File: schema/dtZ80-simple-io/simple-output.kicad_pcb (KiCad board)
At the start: 2 copper layers, 12 parts, among them J1 Conn_01x40, U1 74LS138, U2 74LS573, U3 74LS573, U4 74HC00, U5 HDSP-A151, U6 HDSP-A151

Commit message: Reworked Boards
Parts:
- removed U6: HDSP-A151, Display_7Segment:HDSP-A151
- added C2: 100n, Capacitor_THT:C_Disc_D4.3mm_W1.9mm_P5.00mm, F.Cu at (118.1, 188.0)
- added C3: 22pF, Capacitor_THT:C_Disc_D4.3mm_W1.9mm_P5.00mm, F.Cu at (77.5, 135.9)
- added C4: 100n, Capacitor_THT:C_Disc_D4.3mm_W1.9mm_P5.00mm, F.Cu at (111.8, 130.8)
- added C5: 100n, Capacitor_THT:C_Disc_D4.3mm_W1.9mm_P5.00mm, F.Cu at (54.6, 129.5)
- added C6: 22pF, Capacitor_THT:C_Disc_D4.3mm_W1.9mm_P5.00mm, F.Cu at (85.1, 135.9)
- added IC1: Z80SIO, Package_DIP:DIP-40_W15.24mm_Socket, F.Cu at (52.1, 135.9)
- added IC2: Z80CTC, Package_DIP:DIP-28_W15.24mm_Socket, F.Cu at (91.4, 175.3)
- added J2: 8 Bit Port, Connector_PinHeader_2.54mm:PinHeader_2x07_P2.54mm_Vertical, F.Cu at (55.9, 90.2)
- added J3: FT_232, Connector_PinHeader_2.54mm:PinHeader_1x06_P2.54mm_Vertical, F.Cu at (55.9, 101.6)
- added J4: Mini-DIN-6, package_connectors:Mini_DIN_6_TE_Connectivity, F.Cu at (161.3, 121.9)
- added Jumper1: Conn_01x02, Connector_PinHeader_2.54mm:PinHeader_1x02_P2.54mm_Vertical, F.Cu at (94.0, 106.7)
- added Q1: Q_NPN_BCE, Package_TO_SOT_THT:TO-92_HandSolder, F.Cu at (151.1, 138.4)
- added Q2: Q_NPN_BCE, Package_TO_SOT_THT:TO-92_HandSolder, F.Cu at (151.1, 146.1)
- added R10: 1k, Resistor_THT:R_Axial_DIN0204_L3.6mm_D1.6mm_P5.08mm_Horizontal, F.Cu at (123.2, 181.6)
- added R11: 5K, Resistor_THT:R_Axial_DIN0204_L3.6mm_D1.6mm_P5.08mm_Horizontal, F.Cu at (149.9, 120.7)
- added R12: 5K, Resistor_THT:R_Axial_DIN0204_L3.6mm_D1.6mm_P5.08mm_Horizontal, F.Cu at (149.9, 125.7)
- added R13: 5K, Resistor_THT:R_Axial_DIN0204_L3.6mm_D1.6mm_P5.08mm_Horizontal, F.Cu at (141.0, 142.2)
- added R14: 5K, Resistor_THT:R_Axial_DIN0204_L3.6mm_D1.6mm_P5.08mm_Horizontal, F.Cu at (141.0, 147.3)
- added R5: 10K, Resistor_THT:R_Axial_DIN0204_L3.6mm_D1.6mm_P5.08mm_Horizontal, F.Cu at (78.7, 184.2)
- added R6: 2K, Resistor_THT:R_Axial_DIN0204_L3.6mm_D1.6mm_P5.08mm_Horizontal, F.Cu at (66.0, 113.0)
- added R7: 10K, Resistor_THT:R_Axial_DIN0204_L3.6mm_D1.6mm_P5.08mm_Horizontal, F.Cu at (72.4, 144.8)
- added R8: 2K, Resistor_THT:R_Axial_DIN0204_L3.6mm_D1.6mm_P5.08mm_Horizontal, F.Cu at (61.0, 119.4)
- added R9: 2K, Resistor_THT:R_Axial_DIN0204_L3.6mm_D1.6mm_P5.08mm_Horizontal, F.Cu at (57.1, 108.0)
- added U8: 74HC245, Package_DIP:DIP-20_W7.62mm_Socket, F.Cu at (116.8, 137.2)
- added Y1: Crystal, Crystal:Crystal_HC49-U_Vertical, F.Cu at (99.1, 144.8)
- C1: value 10u -> 100n; footprint Capacitor_THT:CP_Radial_Tantal_D4.5mm_P5.00mm -> Capacitor_THT:C_Disc_D4.3mm_W1.9mm_P5.00mm
- J1: value Conn_01x40 -> RC2014Bus; footprint Connector_PinSocket_2.54mm:PinSocket_1x40_P2.54mm_Horizontal -> Connector_PinHeader_2.54mm:PinHeader_1x40_P2.54mm_Vertical
- R1: footprint Resistor_THT:R_Axial_DIN0204_L3.6mm_D1.6mm_P1.90mm_Vertical -> Resistor_THT:R_Axial_DIN0204_L3.6mm_D1.6mm_P5.08mm_Horizontal
- R2: value 1k -> 220; footprint Resistor_THT:R_Axial_DIN0204_L3.6mm_D1.6mm_P1.90mm_Vertical -> Resistor_THT:R_Axial_DIN0204_L3.6mm_D1.6mm_P5.08mm_Horizontal
- R3: value 220 -> 1M; footprint Resistor_THT:R_Axial_DIN0204_L3.6mm_D1.6mm_P1.90mm_Vertical -> Resistor_THT:R_Axial_DIN0204_L3.6mm_D1.6mm_P5.08mm_Horizontal
- R4: value 220 -> 1K; footprint Resistor_THT:R_Axial_DIN0204_L3.6mm_D1.6mm_P1.90mm_Vertical -> Resistor_THT:R_Axial_DIN0204_L3.6mm_D1.6mm_P5.08mm_Horizontal
- U1: value 74LS138 -> 74LS04; footprint Package_DIP:DIP-16_W7.62mm_Socket -> Package_DIP:DIP-14_W7.62mm_Socket
- U2: value 74LS573 -> 74LS138; footprint Package_DIP:DIP-20_W7.62mm_Socket -> Package_DIP:DIP-16_W7.62mm_Socket
- U4: value 74HC00 -> 74HC245; footprint Package_DIP:DIP-14_W10.16mm -> Package_DIP:DIP-20_W7.62mm_Socket
- U5: value HDSP-A151 -> 5161AS; footprint Display_7Segment:HDSP-A151 -> 7seg:7SegmentLED_LTS6760_LTS6780
- moved J1 147.3 mm to (162.6, 193.0), turned to 270 degrees
- moved U1 87.0 mm to (141.0, 153.7)
- moved U2 86.3 mm to (76.2, 160.0)
- moved R4 67.3 mm to (91.9, 135.9)
- moved C1 65.3 mm to (101.6, 154.9), turned to 0 degrees
- moved R3 62.7 mm to (72.4, 135.9), turned to 90 degrees
- moved U4 50.0 mm to (123.2, 108.0), turned to 180 degrees
- moved U5 36.9 mm to (156.2, 100.3), turned to 90 degrees
- moved R1 21.9 mm to (135.9, 115.6), turned to 270 degrees
- moved U3 15.3 mm to (143.5, 108.0), turned to 180 degrees
- moved R2 13.3 mm to (161.3, 106.7), turned to 180 degrees
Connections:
- C1 pad 2: +5V -> GND
- J1 pad 1: /A15 -> (no net)
- J1 pad 12: Net-(J1-Pad12) -> /A4
- J1 pad 13: /A3 -> (no net)
- J1 pad 14: /A2 -> (no net)
- J1 pad 15: /A1 -> (no net)
- J1 pad 16: /A0 -> (no net)
- J1 pad 17: +5V -> GND
- J1 pad 19: /M1 -> /~M1~
- J1 pad 2: Net-(J1-Pad2) -> (no net)
- J1 pad 20: Net-(J1-Pad20) -> /~RESET~
- J1 pad 22: Net-(J1-Pad22) -> /~INT~
- J1 pad 23: Net-(J1-Pad23) -> (no net)
- J1 pad 24: /WR -> (no net)
- J1 pad 25: /RD -> /~RD~
- J1 pad 26: /IORQ -> /~IORQ~
- J1 pad 28: Net-(J1-Pad28) -> /D1
- J1 pad 29: Net-(J1-Pad29) -> /D2
- J1 pad 3: Net-(J1-Pad3) -> (no net)
- J1 pad 30: Net-(J1-Pad30) -> /D3
- J1 pad 31: Net-(J1-Pad31) -> /D4
- J1 pad 32: Net-(J1-Pad32) -> /D5
- J1 pad 33: Net-(J1-Pad33) -> /D6
- J1 pad 35: Net-(J1-Pad35) -> (no net)
- J1 pad 36: Net-(J1-Pad36) -> (no net)
- J1 pad 37: Net-(J1-Pad37) -> (no net)
- J1 pad 38: Net-(J1-Pad38) -> (no net)
- J1 pad 39: Net-(J1-Pad39) -> (no net)
- J1 pad 4: Net-(J1-Pad4) -> (no net)
- J1 pad 40: Net-(J1-Pad40) -> (no net)
- J1 pad 5: Net-(J1-Pad5) -> (no net)
- J1 pad 6: Net-(J1-Pad6) -> (no net)
- J1 pad 7: Net-(J1-Pad7) -> (no net)
- J1 pad 8: /A8 -> (no net)
- R1 pad 2: +5V -> GND
- R2 pad 2: +5V -> GND
- R3 pad 2: +5V -> Net-(C3-Pad1)
- R4 pad 1: Net-(R4-Pad1) -> Net-(R3-Pad1)
- R4 pad 2: +5V -> Net-(C6-Pad1)
- U1 pad 1: /A5 -> Net-(C3-Pad1)
- U1 pad 11: Net-(U1-Pad11) -> /~Y0~
- U1 pad 12: Net-(U1-Pad12) -> (no net)
- U1 pad 13: Net-(U1-Pad13) -> (no net)
- U1 pad 14: Net-(U1-Pad14) -> +5V
- U1 pad 2: /A6 -> Net-(R3-Pad1)
- U1 pad 3: /A7 -> Net-(R3-Pad1)
- U1 pad 4: /WR -> /CLK7.3728
- U1 pad 5: /IORQ -> /~RD~
- U1 pad 6: /M1 -> /RD
- U1 pad 7: Net-(U1-Pad7) -> GND
- U1 pad 8: +5V -> /Y1
- U1 pad 9: Net-(U1-Pad9) -> /~Y1~
- U2 pad 1: Net-(R1-Pad1) -> /A5
- U2 pad 10: +5V -> (no net)
- U2 pad 11: Net-(U2-Pad11) -> /~Y4~
- U2 pad 12: Net-(U2-Pad12) -> /~Y3~
- U2 pad 13: Net-(U2-Pad13) -> /~Y2~
- U2 pad 14: Net-(U2-Pad14) -> /~Y1~
- U2 pad 15: Net-(U2-Pad15) -> /~Y0~
- U2 pad 16: Net-(U2-Pad16) -> +5V
- U2 pad 2: /D0 -> /A6
- U2 pad 3: Net-(J1-Pad28) -> /A7
- U2 pad 4: Net-(J1-Pad29) -> /A4
- U2 pad 5: Net-(J1-Pad30) -> /~IORQ~
- U2 pad 6: Net-(J1-Pad31) -> /~M1~
- U2 pad 7: Net-(J1-Pad32) -> (no net)
- U2 pad 8: Net-(J1-Pad33) -> GND
- U2 pad 9: /D7 -> (no net)
- U3 pad 1: Net-(R2-Pad1) -> Net-(R1-Pad1)
- U3 pad 10: +5V -> GND
- U3 pad 11: Net-(U3-Pad11) -> Net-(U1-Pad10)
- U3 pad 3: Net-(J1-Pad28) -> /D1
- U3 pad 4: Net-(J1-Pad29) -> /D2
- U3 pad 5: Net-(J1-Pad30) -> /D3
- U3 pad 6: Net-(J1-Pad31) -> /D4
- U3 pad 7: Net-(J1-Pad32) -> /D5
- U3 pad 8: Net-(J1-Pad33) -> /D6
- U4 pad 1: Net-(U1-Pad15) -> /RD
- U4 pad 10: (no net) -> GND
- U4 pad 11: (no net) -> /IO7
- U4 pad 12: (no net) -> /IO6
- U4 pad 13: (no net) -> /IO5
- U4 pad 14: (no net) -> /IO4
- U4 pad 2: Net-(U1-Pad15) -> /D0
- U4 pad 3: Net-(U2-Pad11) -> /D1
- U4 pad 4: Net-(U1-Pad14) -> /D2
- U4 pad 5: Net-(U1-Pad14) -> /D3
- U4 pad 6: Net-(U3-Pad11) -> /D4
- U4 pad 7: (no net) -> /D5
- U4 pad 8: (no net) -> /D6
- U4 pad 9: (no net) -> /D7
- U5 pad 1: Net-(U5-Pad1) -> Net-(U3-Pad15)
- U5 pad 10: Net-(U2-Pad19) -> Net-(U3-Pad13)
- U5 pad 2: Net-(U2-Pad14) -> Net-(U3-Pad16)
- U5 pad 3: Net-(U2-Pad13) -> (no net)
- U5 pad 4: Net-(U2-Pad15) -> Net-(U3-Pad17)
- U5 pad 5: Net-(U2-Pad16) -> Net-(U3-Pad12)
- U5 pad 6: Net-(R3-Pad1) -> Net-(U3-Pad18)
- U5 pad 7: Net-(U2-Pad12) -> Net-(U3-Pad19)
- U5 pad 8: Net-(U2-Pad17) -> Net-(R2-Pad1)
- U5 pad 9: Net-(U2-Pad18) -> Net-(U3-Pad14)
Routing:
- net GND: track 0.00 -> 389.0 mm, vias 0 -> 25
- net +5V: track 58.9 -> 434.5 mm, vias 0 -> 7
- net /Y1: track 0.00 -> 197.5 mm, vias 0 -> 1
- net /D5: track 0.00 -> 176.0 mm, vias 0 -> 3
- net /D3: track 0.00 -> 171.0 mm, vias 0 -> 7
- net Net-(U2-Pad11): track 156.8 -> 0.00 mm
- net /D7: track 39.2 -> 194.0 mm, vias 0 -> 3
- net /D1: track 0.00 -> 151.6 mm, vias 0 -> 12
- net /D6: track 0.00 -> 151.6 mm, vias 0 -> 7
- net /~RD~: track 0.00 -> 148.0 mm, vias 0 -> 10
- net /~Y1~: track 0.00 -> 146.9 mm, vias 0 -> 4
- net /CLK: track 0.00 -> 143.9 mm, vias 0 -> 2
- net /RD: track 0.00 -> 141.9 mm, vias 0 -> 5
- net /D4: track 0.00 -> 137.1 mm, vias 0 -> 8
- net /D2: track 0.00 -> 136.8 mm, vias 0 -> 12
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
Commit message: Schema
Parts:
- added J5: CTC, Connector_PinHeader_2.54mm:PinHeader_1x05_P2.54mm_Vertical, F.Cu at (162.6, 171.4)
- J4: value Mini-DIN-6 -> PS/2 Keyboard
- Q1, Q2: value Q_NPN_BCE -> NPN
- renumbered Jumper1 to J1_5VtoSerial1
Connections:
- IC2 pad 20: (no net) -> Net-(IC2-Pad20)
- IC2 pad 21: (no net) -> Net-(IC2-Pad21)
- IC2 pad 22: (no net) -> Net-(IC2-Pad22)
- IC2 pad 8: (no net) -> Net-(IC2-Pad8)
- IC2 pad 9: (no net) -> Net-(IC2-Pad9)
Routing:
- net /D7: track 194.0 -> 316.0 mm, vias 3 -> 13
- net /D6: track 151.6 -> 251.3 mm, vias 7 -> 13
- net /~Y4~: track 0.00 -> 84.5 mm, vias 0 -> 9
- net /A7: track 0.00 -> 81.1 mm, vias 0 -> 10
- net /D2: track 136.8 -> 209.6 mm, vias 12 -> 20
- net Net-(IC2-Pad21): track 0.00 -> 63.9 mm, vias 0 -> 2
- net Net-(IC2-Pad22): track 0.00 -> 62.7 mm, vias 0 -> 3
- net /D5: track 176.0 -> 238.0 mm, vias 3 -> 10
- net Net-(IC2-Pad20): track 0.00 -> 60.1 mm
- net /~RESET~: track 38.5 -> 97.7 mm, vias 5 -> 8
- net Net-(IC2-Pad9): track 0.00 -> 58.9 mm, vias 0 -> 8
- net /D4: track 137.1 -> 195.5 mm, vias 8 -> 16
- net Net-(IC2-Pad8): track 0.00 -> 55.9 mm, vias 0 -> 4
- net /D1: track 151.6 -> 197.5 mm, vias 12 -> 14
- net /D3: track 171.0 -> 213.4 mm, vias 7 -> 14
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- added copper zone on B.Cu, net GND
- added copper zone on F.Cu, net GND
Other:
- board outline added: 127 x 121.9 mm
- board text added: "1"
- board text added: "CTC"
- board text added: "FTD 232 Serial"
- board text added: "Parallel Port"
- board text added: "dtZ80 IO Board Rev. 1 2021 Stefan Ostermann"

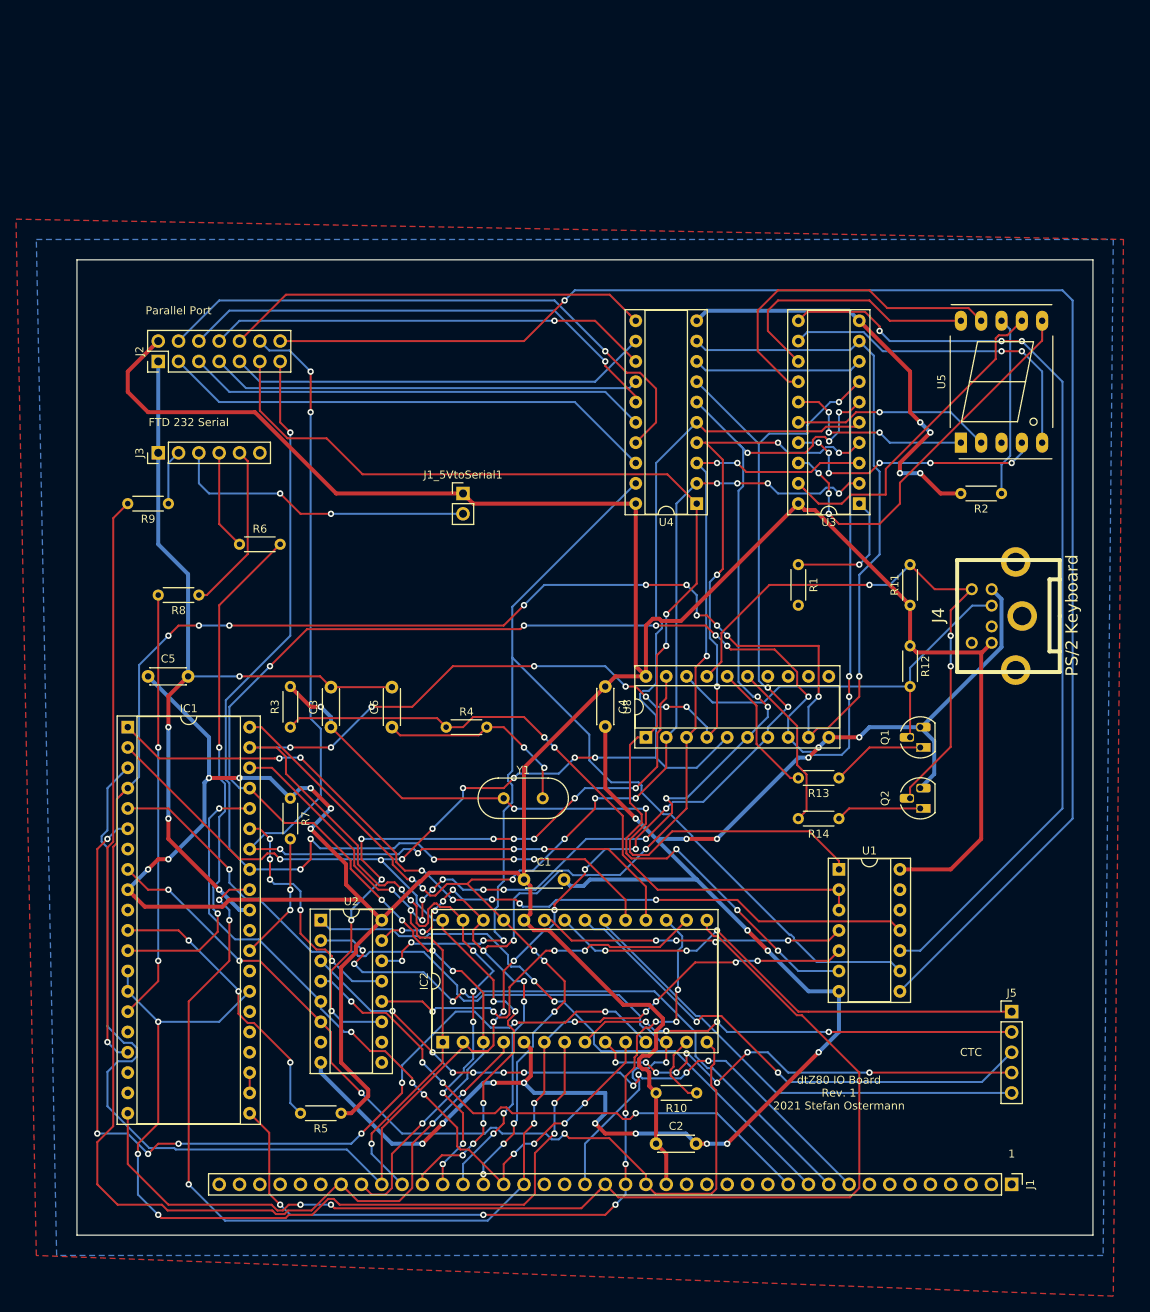
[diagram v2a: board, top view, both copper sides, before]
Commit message: CTC & Fixes on IO Board
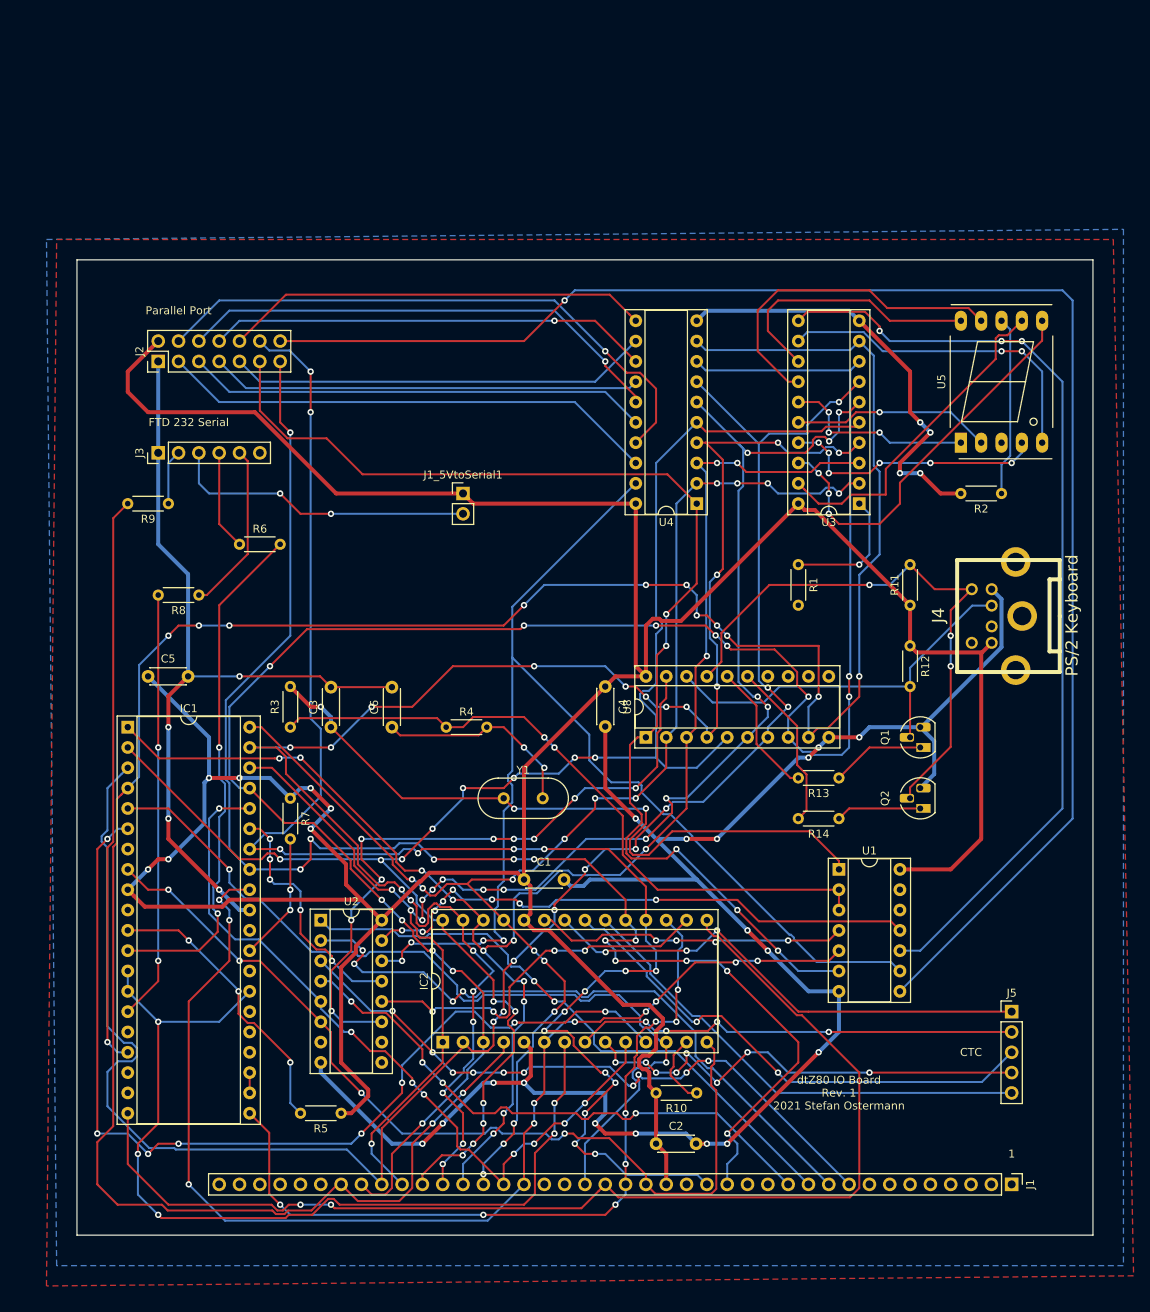
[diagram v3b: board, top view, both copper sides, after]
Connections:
- J1 pad 15: (no net) -> /A1
- J1 pad 16: (no net) -> /A0
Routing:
- net /A0: track 129.8 -> 194.2 mm, vias 6 -> 16
- net /A1: track 124.9 -> 184.4 mm, vias 6 -> 12
- net /A7: track 81.1 -> 81.7 mm
- net /~INT~: track 107.4 -> 108.0 mm
- net /CLK7.3728: track 38.6 -> 39.2 mm
- net /A6: track 82.0 -> 82.6 mm
- net /A4: track 71.1 -> 71.7 mm
